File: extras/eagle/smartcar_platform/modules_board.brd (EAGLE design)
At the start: 140.1 x 77.5 mm, 40 parts

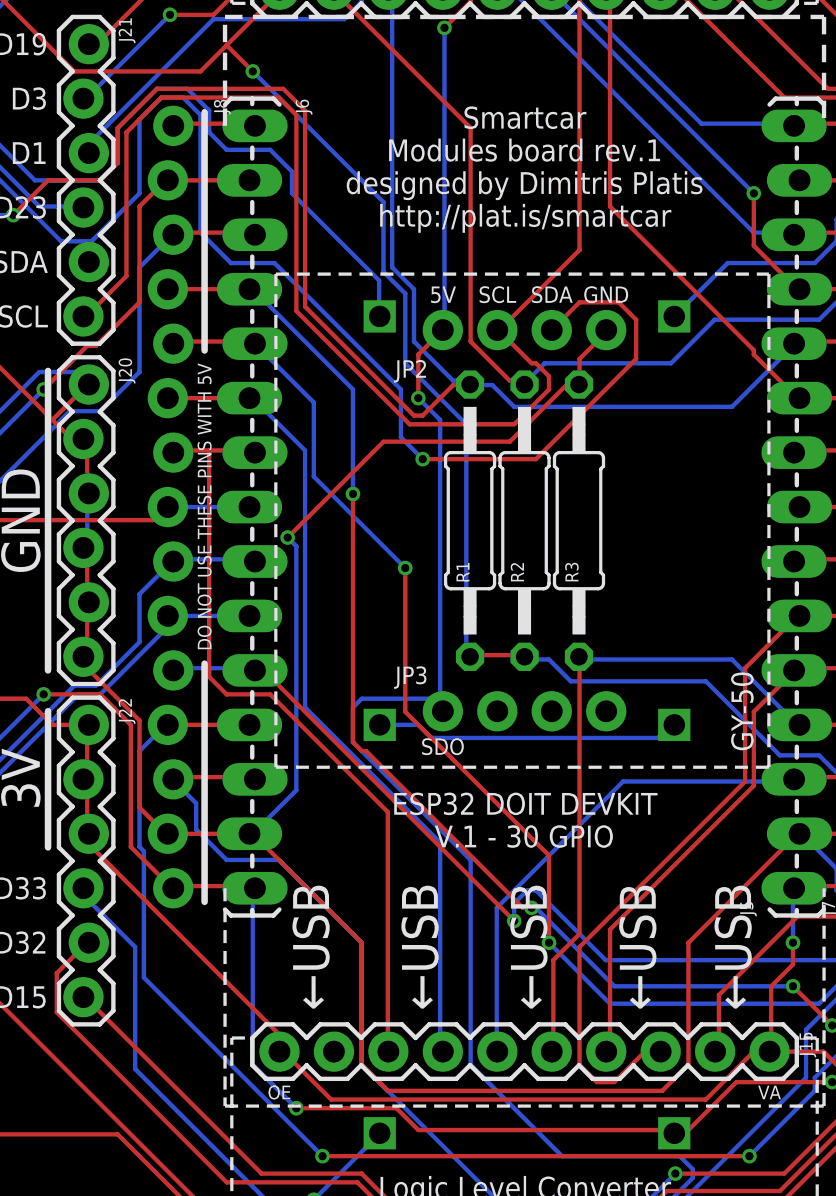
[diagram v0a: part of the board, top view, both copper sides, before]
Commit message: Fix ESP32 power supply line to 5V
ESP32 was powered on via its VIN pin which based
on the specs of the ESP32 DOIT devkit is supposed
to handle up to 12V.
This isn't actually the case and anything above 6V
makes the regulator on the board overheat.

Note that the 5V is actually the voltage coming from
our own on-board regulator.
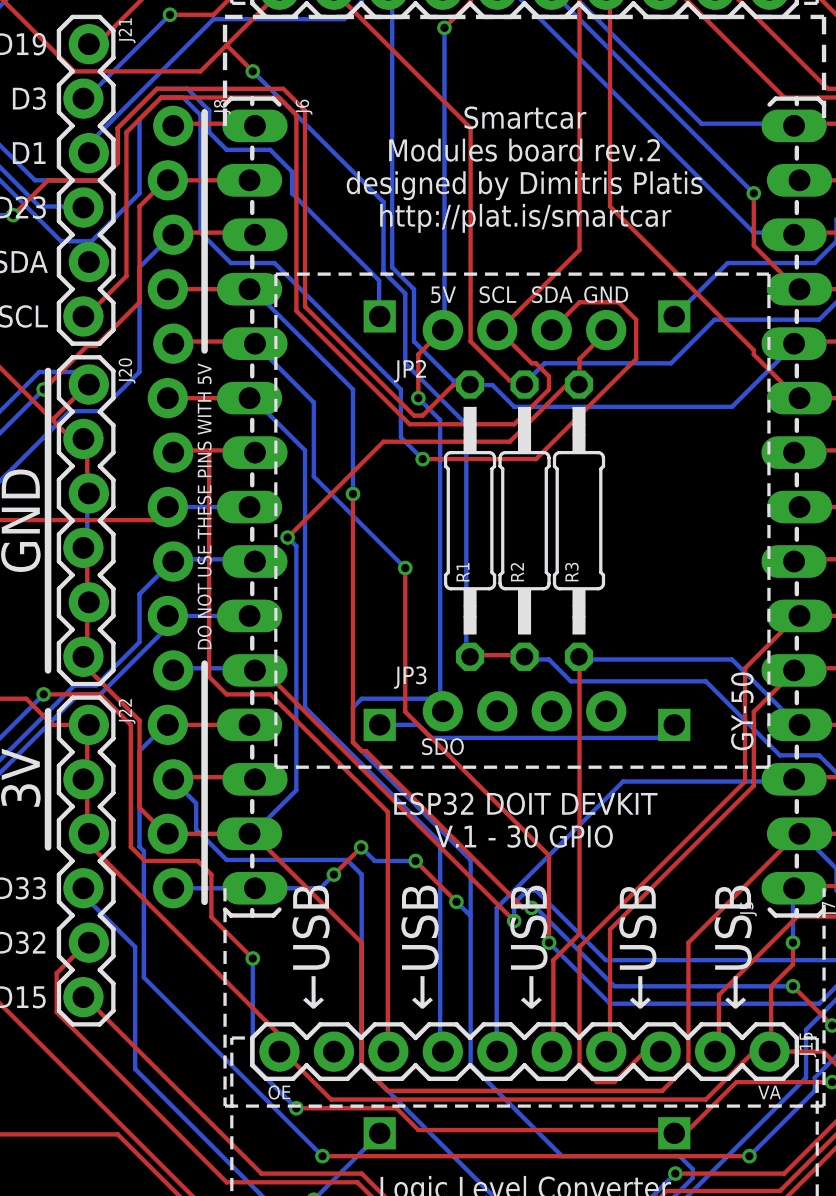
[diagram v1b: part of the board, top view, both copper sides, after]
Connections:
- net 5V: now also J6.15, J8.15
- net MOTOR_VCC: no longer J6.15, J8.15
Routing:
- net 5V: track 208.4 -> 224.4 mm, vias 5 -> 9
- net MOTOR_R_EN: track 99.6 -> 101.5 mm
- net MOTOR_VCC: track 214.1 -> 213.1 mm, vias 5 -> 6
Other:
- board text added: "Smartcar Modules board rev.2 designed by Dimitris Platis http://plat.is/smartcar"
- board text removed: "Smartcar Modules board rev.1 designed by Dimitris Platis http://plat.is/smartcar"
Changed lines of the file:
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@@
 <?xml version="1.0" encoding="utf-8"?>
 <!DOCTYPE eagle SYSTEM "eagle.dtd">
-<eagle version="9.5.2">
+<eagle version="9.6.2">
 <drawing>
 <settings>
-<setting alwaysvectorfont="yes"/>
+<setting alwaysvectorfont="no"/>
 <setting verticaltext="up"/>
 </settings>
@@
 V.1 - 30 GPIO</text>
 <text x="98.425" y="76.835" size="1.016" layer="21" font="vector" rot="SR0" align="center">Smartcar
-Modules board rev.1
+Modules board rev.2
 designed by Dimitris Platis
 http://plat.is/smartcar</text>
@@
 <contactref element="J4" pad="2"/>
 <contactref element="J2" pad="3"/>
-<contactref element="J6" pad="15"/>
 <contactref element="5V_REGULATOR" pad="1"/>
-<contactref element="J8" pad="15"/>
 <contactref element="BAT8" pad="POS"/>
 <wire x1="161.3408" y1="29.8704" x2="161.3408" y2="29.2608" width="0.2032" layer="16"/>
@@
 <wire x1="87.7824" y1="32.9184" x2="92.456" y2="32.9184" width="0.2032" layer="1"/>
 <wire x1="85.7504" y1="34.9504" x2="87.7824" y2="32.9184" width="0.2032" layer="16"/>
-<wire x1="85.7504" y1="43.0784" x2="85.7504" y2="34.9504" width="0.2032" layer="16"/>
+<wire x1="85.7504" y1="39.9034" x2="85.7504" y2="34.9504" width="0.2032" layer="16"/>
 <wire x1="105.2576" y1="31.9024" x2="105.41" y2="31.75" width="0.2032" layer="1"/>
-<wire x1="85.7504" y1="43.0784" x2="85.852" y2="43.18" width="0.2032" layer="16"/>
 <wire x1="34.7472" y1="30.0736" x2="34.7472" y2="29.2608" width="0.2032" layer="16"/>
 <wire x1="33.528" y1="31.2928" x2="34.7472" y2="30.0736" width="0.2032" layer="16"/>
@@
 <wire x1="78.6384" y1="52.2224" x2="75.9968" y2="52.2224" width="0.2032" layer="1"/>
 <wire x1="80.0608" y1="50.8" x2="78.6384" y2="52.2224" width="0.2032" layer="1"/>
-<wire x1="80.0608" y1="45.1104" x2="80.0608" y2="50.8" width="0.2032" layer="1"/>
-<wire x1="81.8896" y1="43.2816" x2="80.0608" y2="45.1104" width="0.2032" layer="1"/>
+<wire x1="80.0608" y1="50.8" x2="80.0608" y2="45.1104" width="0.2032" layer="1"/>
 <wire x1="34.7472" y1="29.2608" x2="34.925" y2="29.21" width="0.2032" layer="16"/>
-<wire x1="81.8896" y1="43.2816" x2="82.042" y2="43.18" width="0.2032" layer="1"/>
-<wire x1="82.0928" y1="43.2816" x2="85.7504" y2="43.2816" width="0.2032" layer="1"/>
-<wire x1="85.7504" y1="43.2816" x2="85.852" y2="43.18" width="0.2032" layer="1"/>
-<wire x1="82.0928" y1="43.2816" x2="82.042" y2="43.18" width="0.2032" layer="1"/>
 <wire x1="124.7648" y1="29.2608" x2="161.1376" y2="29.2608" width="0.2032" layer="1"/>
 <wire x1="124.3584" y1="29.2608" x2="124.7648" y2="29.2608" width="0.2032" layer="16"/>
@@
 <via x="124.7648" y="29.2608" extent="1-16" drill="0.381"/>
 <via x="112.776" y="34.1376" extent="1-16" drill="0.381"/>
+<wire x1="80.0608" y1="45.1104" x2="80.7212" y2="44.45" width="0.2032" layer="1"/>
+<wire x1="80.7212" y1="44.45" x2="83.185" y2="44.45" width="0.2032" layer="1"/>
+<wire x1="83.185" y1="44.45" x2="83.82" y2="43.815" width="0.2032" layer="1"/>
+<wire x1="83.82" y1="41.8338" x2="85.7504" y2="39.9034" width="0.2032" layer="1"/>
+<via x="85.7504" y="39.9034" extent="1-16" drill="0.381"/>
+<wire x1="83.82" y1="43.815" x2="83.82" y2="41.8338" width="0.2032" layer="1"/>
 </signal>
 <signal name="MOTOR_R_IN1">
@@
 <wire x1="99.568" y1="26.2128" x2="103.2256" y2="26.2128" width="0.2032" layer="16"/>
 <wire x1="90.8304" y1="34.9504" x2="99.568" y2="26.2128" width="0.2032" layer="16"/>
-<wire x1="90.8304" y1="40.64" x2="90.8304" y2="34.9504" width="0.2032" layer="16"/>
-<wire x1="86.9696" y1="44.5008" x2="90.8304" y2="40.64" width="0.2032" layer="16"/>
-<wire x1="84.5312" y1="44.5008" x2="86.9696" y2="44.5008" width="0.2032" layer="16"/>
+<wire x1="90.8304" y1="43.815" x2="90.8304" y2="34.9504" width="0.2032" layer="16"/>
+<wire x1="90.1446" y1="44.5008" x2="90.8304" y2="43.815" width="0.2032" layer="16"/>
+<wire x1="84.5312" y1="44.5008" x2="90.1446" y2="44.5008" width="0.2032" layer="16"/>
 <wire x1="83.1088" y1="45.9232" x2="84.5312" y2="44.5008" width="0.2032" layer="16"/>
 <wire x1="83.1088" y1="47.1424" x2="83.1088" y2="45.9232" width="0.2032" layer="16"/>
@@
 <wire x1="100.1776" y1="30.6832" x2="105.664" y2="30.6832" width="0.2032" layer="16"/>
 <wire x1="95.9104" y1="34.9504" x2="100.1776" y2="30.6832" width="0.2032" layer="16"/>
-<wire x1="95.9104" y1="44.5008" x2="95.9104" y2="34.9504" width="0.2032" layer="16"/>
+<wire x1="95.9104" y1="44.5008" x2="95.9104" y2="41.91" width="0.2032" layer="16"/>
+<wire x1="95.9104" y1="41.91" x2="95.9104" y2="34.9504" width="0.2032" layer="16"/>
 <wire x1="90.424" y1="49.9872" x2="95.9104" y2="44.5008" width="0.2032" layer="16"/>
 <wire x1="90.424" y1="51.6128" x2="90.424" y2="49.9872" width="0.2032" layer="16"/>
@@
 <via x="94.6912" y="83.312" extent="1-16" drill="0.381"/>
 <via x="95.9104" y="87.9856" extent="1-16" drill="0.381"/>
+<contactref element="J8" pad="15"/>
+<contactref element="J6" pad="15"/>
+<wire x1="95.9104" y1="41.91" x2="95.885" y2="41.91" width="0.2032" layer="16"/>
+<wire x1="95.885" y1="41.91" x2="95.25" y2="42.545" width="0.2032" layer="16"/>
+<via x="95.25" y="42.545" extent="1-16" drill="0.381"/>
+<wire x1="95.25" y1="42.545" x2="93.345" y2="44.45" width="0.2032" layer="1"/>
+<via x="93.345" y="44.45" extent="1-16" drill="0.381"/>
+<wire x1="93.345" y1="44.45" x2="91.44" y2="44.45" width="0.2032" layer="16"/>
+<wire x1="91.44" y1="44.45" x2="90.805" y2="45.085" width="0.2032" layer="16"/>
+<via x="90.805" y="45.085" extent="1-16" drill="0.381"/>
+<wire x1="90.805" y1="45.085" x2="89.535" y2="43.815" width="0.2032" layer="1"/>
+<via x="89.535" y="43.815" extent="1-16" drill="0.381"/>
+<wire x1="89.535" y1="43.815" x2="88.9" y2="43.18" width="0.2032" layer="16"/>
+<wire x1="88.9" y1="43.18" x2="85.852" y2="43.18" width="0.2032" layer="16"/>
+<wire x1="85.852" y1="43.18" x2="82.042" y2="43.18" width="0.2032" layer="16"/>
 </signal>
 <signal name="N$2">
